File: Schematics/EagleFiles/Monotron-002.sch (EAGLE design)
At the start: 52 parts, among them IC1 LM324D, J1 pitch_CV, J2 gate_CV, J3 cutoff_CV, J4 LFO, Q1 N-MOSFET, U1 TPS2105D, X1 MICRO-USB-RECEPTACLE47589-0001

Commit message: updated schematics and brd files
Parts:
- R2: value 47k -> 10k
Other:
- note added: "I(Q1) < 0.2mA for maximum inputs"
- note added: "~0.9V"
- note removed: "Vgs max < 4V RdsON as low as possible"
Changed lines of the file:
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@@
 <part name="R17" library="Mage-Control" deviceset="R-EU" device="R0603" value="47k"/>
 <part name="R1" library="Mage-Control" deviceset="R-EU" device="R0603" value="47k"/>
-<part name="R2" library="Mage-Control" deviceset="R-EU" device="R0603" value="47k"/>
+<part name="R2" library="Mage-Control" deviceset="R-EU" device="R0603" value="10k"/>
 <part name="R4" library="Mage-Control" deviceset="R-EU" device="R0603" value="47k"/>
 <part name="R5" library="Mage-Control" deviceset="R-EU" device="R0603" value="33k"/>
@@
 unless stated otherwise</text>
 <text x="129.54" y="241.3" size="5.08" layer="136">Eurorack-monotron interface</text>
-<text x="170.18" y="124.46" size="1.778" layer="136">Vgs max &lt; 4V
-RdsON as low as possible</text>
 <text x="134.62" y="177.8" size="1.778" layer="136">Desired output: 0.44V/oct</text>
 <text x="144.78" y="228.6" size="1.778" layer="136">Desired output: 1.56V</text>
@@
 <text x="30.48" y="30.48" size="1.778" layer="97">Do not place JACKS too close to each other,
 as the connectors are wider than the plugs and might not fit</text>
+<text x="165.1" y="127" size="1.778" layer="136">I(Q1) &lt; 0.2mA for maximum inputs</text>
+<text x="71.12" y="101.6" size="1.778" layer="136">~0.9V</text>
 </plain>
 <instances>

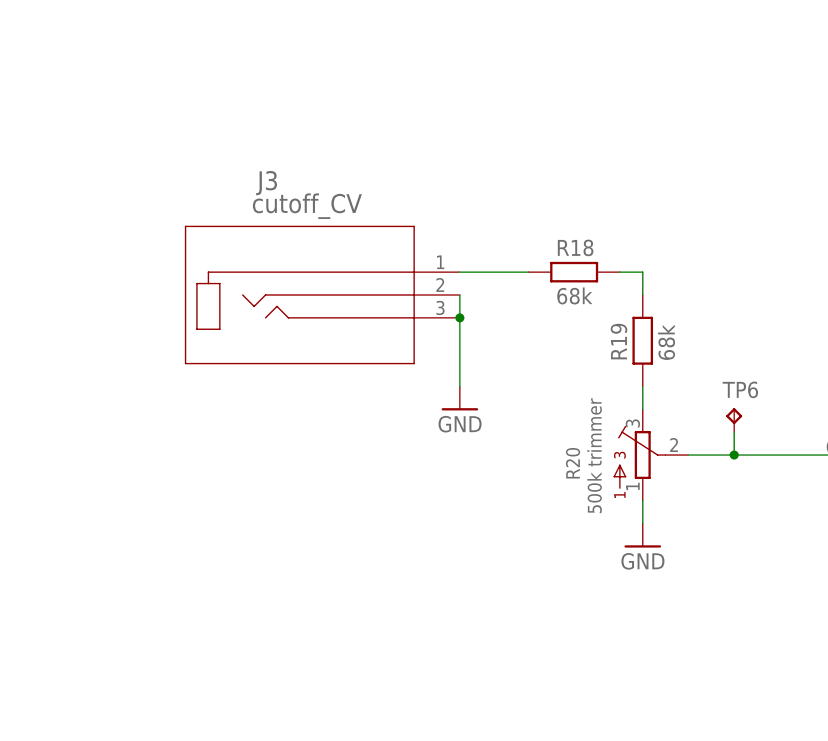
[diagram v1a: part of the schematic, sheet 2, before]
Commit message: updated eagle files
corrected cutoff connector wiring and cutoff trimmer disconnected from GND
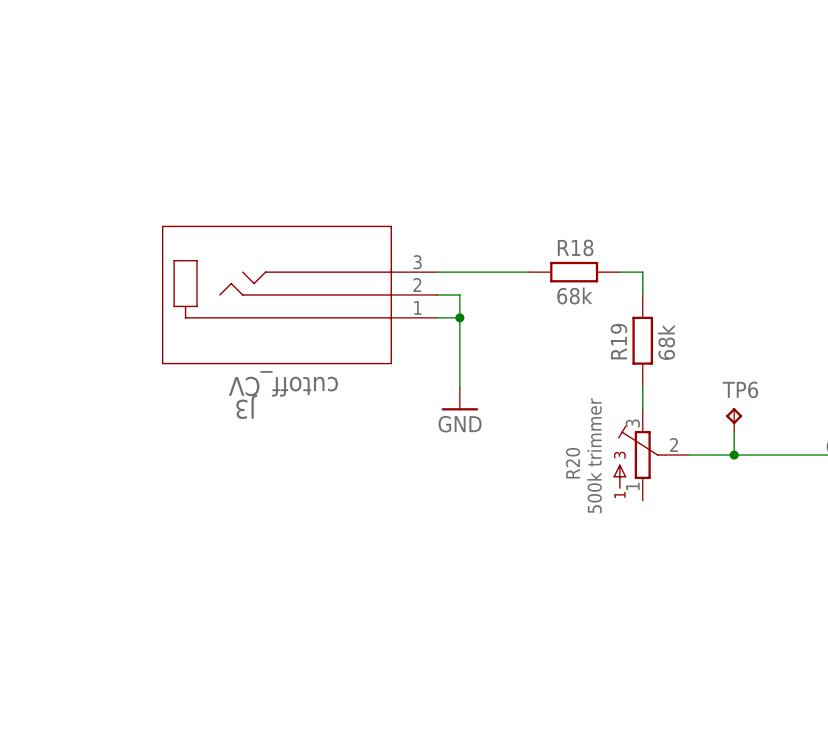
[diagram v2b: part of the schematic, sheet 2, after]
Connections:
- removed net N$8: J3.1, R18.2
- new net N$6: J3.3, R18.2
- net GND: now also J3.1; no longer J3.3, R20.1
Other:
- moved on the sheet: J3
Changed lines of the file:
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@@
 <part name="R12" library="bourns" deviceset="3362" device="R" value="10k trimmer"/>
 <part name="R20" library="bourns" deviceset="3362" device="R" value="500k trimmer"/>
-<part name="GND14" library="supply1" library_urn="urn:adsk.eagle:library:371" deviceset="GND" device=""/>
 <part name="GND15" library="supply1" library_urn="urn:adsk.eagle:library:371" deviceset="GND" device=""/>
 <part name="GND16" library="supply1" library_urn="urn:adsk.eagle:library:371" deviceset="GND" device=""/>
@@
 <attribute name="VALUE" x="40.3606" y="51.8414" size="2.0828" layer="96" ratio="6" rot="SMR180"/>
 </instance>
-<instance part="J3" gate="A" x="297.18" y="99.06" smashed="yes">
-<attribute name="NAME" x="272.1356" y="108.1786" size="2.0828" layer="95" ratio="6" rot="SR0"/>
-<attribute name="VALUE" x="271.5006" y="105.6386" size="2.0828" layer="96" ratio="6" rot="SR0"/>
+<instance part="J3" gate="A" x="294.64" y="93.98" smashed="yes" rot="MR180">
+<attribute name="NAME" x="269.5956" y="84.8614" size="2.0828" layer="95" ratio="6" rot="SMR180"/>
+<attribute name="VALUE" x="268.9606" y="87.4014" size="2.0828" layer="96" ratio="6" rot="SMR180"/>
 </instance>
 <instance part="GND8" gate="1" x="60.96" y="162.56" smashed="yes" rot="MR0">
@@
 <attribute name="NAME" x="307.975" y="75.946" size="1.524" layer="95" ratio="10" rot="R90"/>
 <attribute name="VALUE" x="310.388" y="72.136" size="1.524" layer="96" ratio="10" rot="R90"/>
-</instance>
-<instance part="GND14" gate="1" x="314.96" y="68.58" smashed="yes" rot="MR0">
-<attribute name="VALUE" x="317.5" y="66.04" size="1.778" layer="96" rot="MR0"/>
 </instance>
 <instance part="GND15" gate="1" x="111.76" y="195.58" smashed="yes" rot="MR0">
@@
 <pinref part="R17" gate="G$1" pin="2"/>
 <wire x1="210.82" y1="134.62" x2="210.82" y2="137.16" width="0.1524" layer="91"/>
-</segment>
-<segment>
-<pinref part="J3" gate="A" pin="2"/>
-<wire x1="294.64" y1="96.52" x2="294.64" y2="93.98" width="0.1524" layer="91"/>
-<pinref part="J3" gate="A" pin="3"/>
-<wire x1="294.64" y1="93.98" x2="294.64" y2="86.36" width="0.1524" layer="91"/>
-<junction x="294.64" y="93.98"/>
-<pinref part="GND11" gate="1" pin="GND"/>
 </segment>
 <segment>
@@
 </segment>
 <segment>
-<pinref part="GND14" gate="1" pin="GND"/>
-<pinref part="R20" gate="G$1" pin="1"/>
-<wire x1="314.96" y1="71.12" x2="314.96" y2="73.66" width="0.1524" layer="91"/>
-</segment>
-<segment>
 <pinref part="GND15" gate="1" pin="GND"/>
 <pinref part="R13" gate="G$1" pin="1"/>
@@
 <pinref part="Q1" gate="G$1" pin="S"/>
 <wire x1="177.8" y1="137.16" x2="177.8" y2="139.7" width="0.1524" layer="91"/>
+</segment>
+<segment>
+<pinref part="GND11" gate="1" pin="GND"/>
+<wire x1="294.64" y1="86.36" x2="294.64" y2="93.98" width="0.1524" layer="91"/>
+<pinref part="J3" gate="A" pin="1"/>
+<wire x1="294.64" y1="93.98" x2="292.1" y2="93.98" width="0.1524" layer="91"/>
+<wire x1="294.64" y1="93.98" x2="294.64" y2="96.52" width="0.1524" layer="91"/>
+<junction x="294.64" y="93.98"/>
+<pinref part="J3" gate="A" pin="2"/>
+<wire x1="294.64" y1="96.52" x2="292.1" y2="96.52" width="0.1524" layer="91"/>
 </segment>
 </net>
@@
 <pinref part="IC1" gate="B" pin="OUT"/>
 <wire x1="203.2" y1="165.1" x2="210.82" y2="165.1" width="0.1524" layer="91"/>
-</segment>
-</net>
-<net name="N$8" class="0">
-<segment>
-<pinref part="J3" gate="A" pin="1"/>
-<pinref part="R18" gate="G$1" pin="2"/>
-<wire x1="294.64" y1="99.06" x2="302.26" y2="99.06" width="0.1524" layer="91"/>
 </segment>
 </net>
@@
 </segment>
 </net>
+<net name="N$6" class="0">
+<segment>
+<pinref part="R18" gate="G$1" pin="2"/>
+<pinref part="J3" gate="A" pin="3"/>
+<wire x1="302.26" y1="99.06" x2="292.1" y2="99.06" width="0.1524" layer="91"/>
+</segment>
+</net>
